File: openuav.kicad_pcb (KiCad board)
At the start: 4 copper layers, 36 x 36 mm, 75 parts, among them J1 Conn_01x01, J10 Conn_01x01, J11 Conn_01x01, J12 Conn_01x01, J13 Conn_01x01, J14 Conn_01x01, J15 Conn_01x01, J16 Conn_01x01, J17 Conn_01x01, J18 Conn_01x01, J19 Conn_01x01, J2 Conn_01x01, J20 Conn_01x01, J21 Conn_01x01, J22 Conn_01x01, J23 Conn_01x01, J24 Conn_01x01, J25 Conn_01x01, J26 Conn_01x01, J27 Conn_01x01, J28 Conn_01x01, J3 Conn_01x01, J30 Conn_01x01, J31 Conn_01x01, J4 Conn_01x01, J5 Conn_01x01, J6 Conn_01x01, J7 Conn_01x01, J8 Conn_01x01, J9 Conn_01x01, J99 USB_C_Receptacle_USB2.0, SW1 SW_Push, SW2 SW_Push, U1 STM32G431CBUx, U2 LPS22HH, U3 LSM6DSR, U4 TPS54302, U6 W25N01GVZEIG, U7 TLV75733PDBV

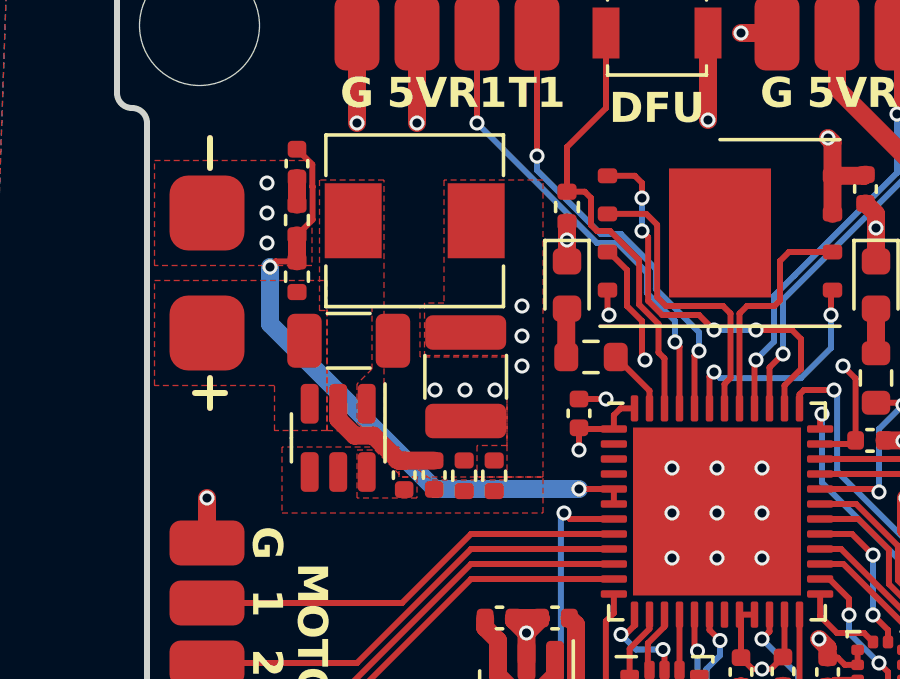
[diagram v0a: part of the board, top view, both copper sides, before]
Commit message: Fix layout for SMPS feedback capacitor
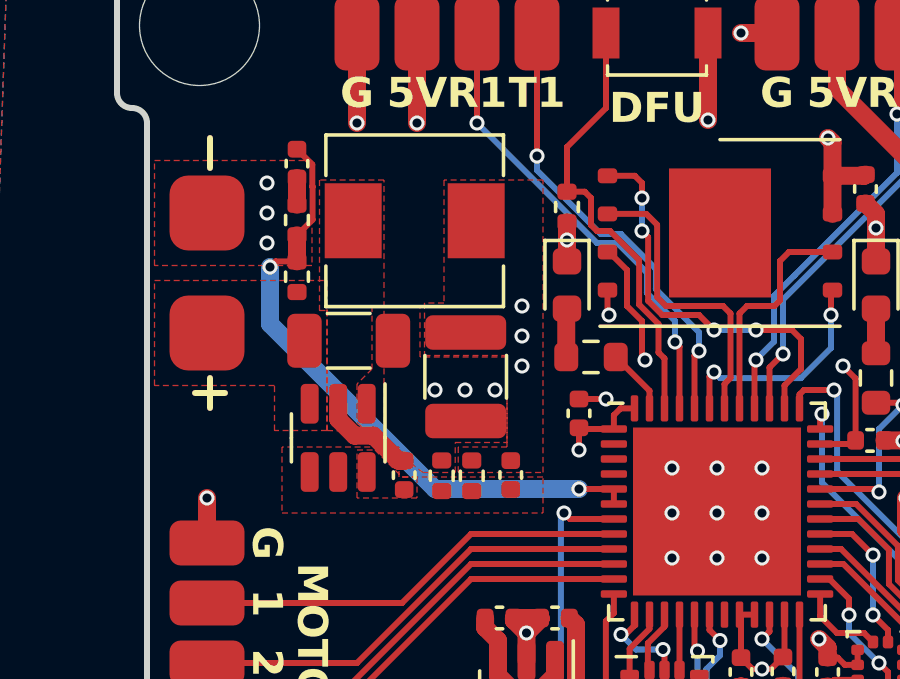
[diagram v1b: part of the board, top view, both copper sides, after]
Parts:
- moved C10 2.55 mm to (143.1, 67.7)
- moved R3 0.75 mm to (141.8, 67.8)
- moved R4 0.75 mm to (140.8, 67.8)
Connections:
- C10 pad 2: Net-(U4-SW) -> +5V
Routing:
- net Net-(U4-SW): track 4.29 -> 3.30 mm
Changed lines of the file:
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@@
   )
   (footprint "Resistor_SMD:R_0402_1005Metric" (layer "F.Cu")
-    (at 141.573 67.758789 90)
+    (at 140.825 67.758789 90)
     (descr "Resistor SMD 0402 (1005 Metric), square (rectangular) end terminal, IPC_7351 nominal, (Body size source: IPC-SM-782 page 72, https://www.pcb-3d.com/wordpress/wp-content/uploads/ipc-sm-782a_amendment_1_and_2.pdf), generated with kicad-footprint-generator")
     (tags "resistor")
@@
   )
   (footprint "Resistor_SMD:R_0402_1005Metric" (layer "F.Cu")
-    (at 142.573 67.758789 -90)
+    (at 141.825 67.758789 -90)
     (descr "Resistor SMD 0402 (1005 Metric), square (rectangular) end terminal, IPC_7351 nominal, (Body size source: IPC-SM-782 page 72, https://www.pcb-3d.com/wordpress/wp-content/uploads/ipc-sm-782a_amendment_1_and_2.pdf), generated with kicad-footprint-generator")
     (tags "resistor")
@@
   )
   (footprint "Capacitor_SMD:C_0402_1005Metric" (layer "F.Cu")
-    (at 140.573 67.733789 90)
+    (at 143.125 67.733789 90)
     (descr "Capacitor SMD 0402 (1005 Metric), square (rectangular) end terminal, IPC_7351 nominal, (Body size source: IPC-SM-782 page 76, https://www.pcb-3d.com/wordpress/wp-content/uploads/ipc-sm-782a_amendment_1_and_2.pdf), generated with kicad-footprint-generator")
     (tags "capacitor")
@@
       (net 7 "Net-(U4-FB)") (pintype "passive"))
     (pad "2" smd roundrect (at 0.48 0 90) (size 0.56 0.62) (layers "F.Cu" "F.Paste" "F.Mask") (roundrect_rratio 0.25)
-      (net 6 "Net-(U4-SW)") (pintype "passive"))
+      (net 9 "+5V") (pintype "passive"))
     (model "${KICAD6_3DMODEL_DIR}/Capacitor_SMD.3dshapes/C_0402_1005Metric.wrl"
       (offset (xyz 0 0 0))
@@
   (segment (start 139.388317 67.258789) (end 138.550817 66.421289) (width 0.6) (layer "F.Cu") (net 6))
   (segment (start 139.578 67.253789) (end 139.573 67.258789) (width 0.6) (layer "F.Cu") (net 6))
-  (segment (start 140.573 67.253789) (end 139.578 67.253789) (width 0.6) (layer "F.Cu") (net 6))
   (segment (start 137.921289 66.421289) (end 137.373 65.873) (width 0.6) (layer "F.Cu") (net 6))
   (segment (start 136 60.613789) (end 135.286211 60.613789) (width 0.2) (layer "F.Cu") (net 8))
@@
         (xy 140.25 63.75)
         (xy 143 63.75)
-        (xy 143 66.75)
-        (xy 142 66.75)
-        (xy 142 67.8)
-        (xy 144.2 67.8)
+        (xy 143 66.8)
+        (xy 141.375 66.8)
+        (xy 141.375 67.65)
+        (xy 144.2 67.65)
       )
     )
@@
         (xy 138 64.7)
         (xy 138 66)
-        (xy 140.5 67.9)
-        (xy 143 67.9)
+        (xy 140.2 67.65)
+        (xy 141.275 67.65)
+        (xy 141.275 66.65)
+        (xy 143 66.65)
         (xy 143 63.8)
         (xy 140.1 63.8)

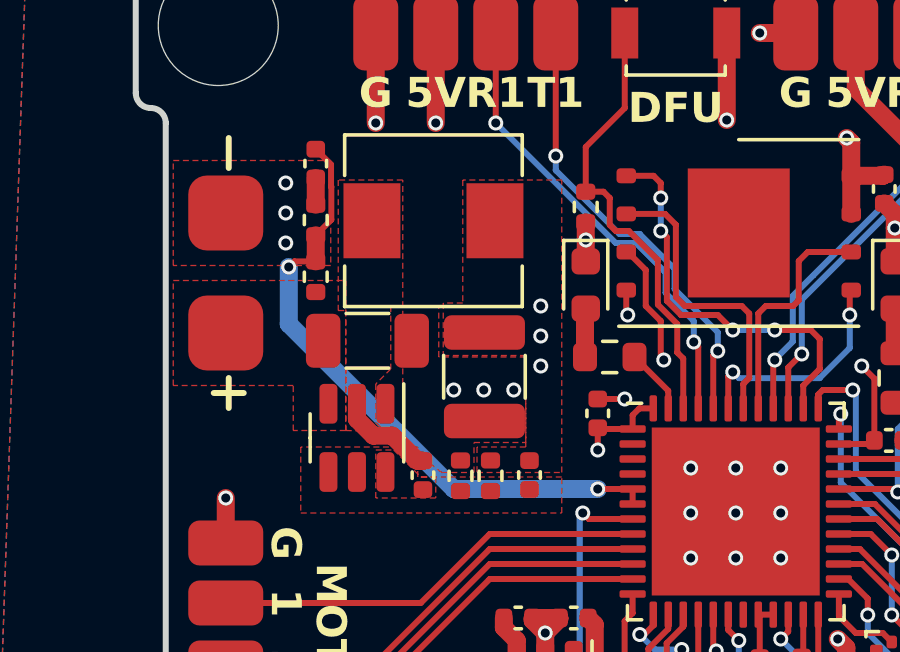
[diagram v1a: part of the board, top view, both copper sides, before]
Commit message: remove copper under inductor
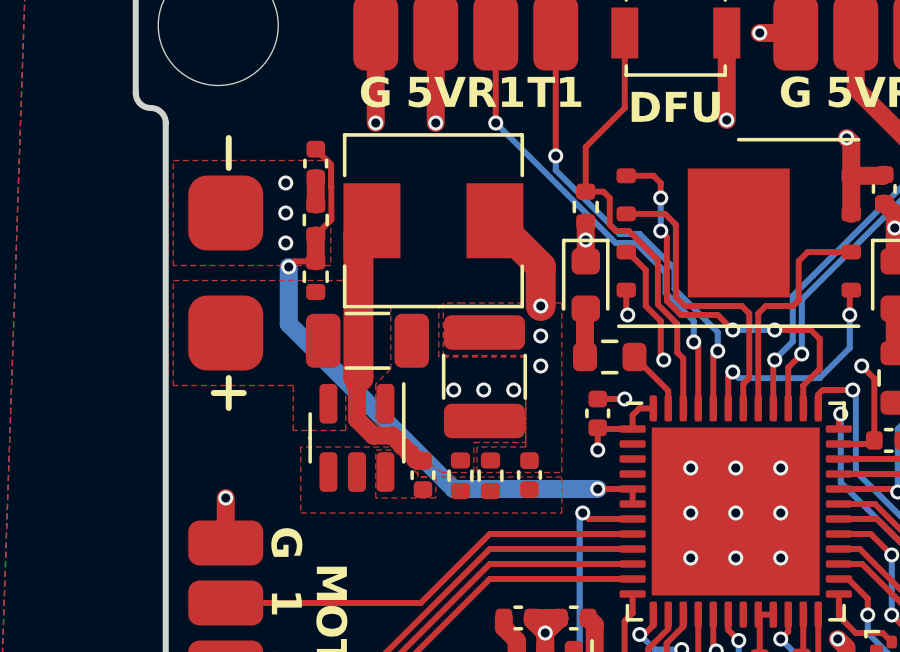
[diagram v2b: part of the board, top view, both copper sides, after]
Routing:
- net Net-(U4-SW): track 3.30 -> 8.70 mm
- net +5V: track 19.5 -> 23.0 mm
- removed copper zone on F.Cu, net Net-(U4-SW)
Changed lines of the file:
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@@
   (segment (start 138.550817 66.421289) (end 137.921289 66.421289) (width 0.6) (layer "F.Cu") (net 6))
   (segment (start 137.373 65.873) (end 137.373 65.358789) (width 0.6) (layer "F.Cu") (net 6))
+  (segment (start 137.423 64.473) (end 137.425 64.475) (width 1) (layer "F.Cu") (net 6))
+  (segment (start 137.873 59.258789) (end 137.423 59.708789) (width 1) (layer "F.Cu") (net 6))
   (segment (start 139.388317 67.258789) (end 138.550817 66.421289) (width 0.6) (layer "F.Cu") (net 6))
   (segment (start 139.578 67.253789) (end 139.573 67.258789) (width 0.6) (layer "F.Cu") (net 6))
+  (segment (start 137.423 59.708789) (end 137.423 64.473) (width 1) (layer "F.Cu") (net 6))
   (segment (start 137.921289 66.421289) (end 137.373 65.873) (width 0.6) (layer "F.Cu") (net 6))
   (segment (start 136 60.613789) (end 135.286211 60.613789) (width 0.2) (layer "F.Cu") (net 8))
@@
   (segment (start 145.4 68.2) (end 140.6 68.2) (width 0.6) (layer "B.Cu") (net 8))
   (segment (start 142.7 73.925) (end 142.7 74.415317) (width 0.6) (layer "F.Cu") (net 9))
+  (segment (start 143.5 60.785789) (end 141.973 59.258789) (width 1) (layer "F.Cu") (net 9))
   (segment (start 144.6 74.415317) (end 144.6 73.925) (width 0.6) (layer "F.Cu") (net 9))
   (segment (start 142.7 73.25) (end 142.7 73.925) (width 0.6) (layer "F.Cu") (net 9))
@@
   (segment (start 140 53) (end 140 56) (width 0.6) (layer "F.Cu") (net 9))
   (segment (start 154 54.85) (end 157.25 58.1) (width 0.6) (layer "F.Cu") (net 9))
+  (segment (start 143.5 62.1) (end 143.5 60.785789) (width 1) (layer "F.Cu") (net 9))
   (segment (start 150 83) (end 150 80.7) (width 0.6) (layer "F.Cu") (net 9))
   (segment (start 144.027817 74.9875) (end 144.6 74.415317) (width 0.6) (layer "F.Cu") (net 9))
@@
     )
   )
-  (zone (net 6) (net_name "Net-(U4-SW)") (layer "F.Cu") (hatch edge 0.5)
-    (priority 2)
-    (connect_pads yes (clearance 0.2))
-    (min_thickness 0.25) (filled_areas_thickness no)
-    (fill yes (thermal_gap 0.5) (thermal_bridge_width 0.5) (smoothing fillet) (radius 0.5))
-    (polygon
-      (pts
-        (xy 138.9 57.9)
-        (xy 136.75 57.9)
-        (xy 136.75 62.25)
-        (xy 137 62.25)
-        (xy 137 66.25)
-        (xy 138.9 66.3)
-      )
-    )
-  )
   (zone (net 3) (net_name "+BATT") (layer "F.Cu") (hatch edge 0.5)
     (priority 1)
@@
     (polygon
       (pts
-        (xy 144.2 57.9)
-        (xy 140.9 57.9)
+        (xy 144.2 62)
         (xy 140.9 62)
         (xy 140.25 62)
@@
       )
     )
+  )
+  (zone (net 0) (net_name "") (layers "F.Cu" "In1.Cu" "In2.Cu" "B.Cu") (hatch edge 0.5)
+    (connect_pads (clearance 0))
+    (min_thickness 0.25) (filled_areas_thickness no)
+    (keepout (tracks allowed) (vias allowed) (pads allowed) (copperpour not_allowed) (footprints allowed))
+    (fill (thermal_gap 0.5) (thermal_bridge_width 0.5))
+    (polygon
+      (pts
+        (xy 136.975 56.425)
+        (xy 136.975 62.1)
+        (xy 142.875 62.1)
+        (xy 142.875 56.425)
+      )
+    )

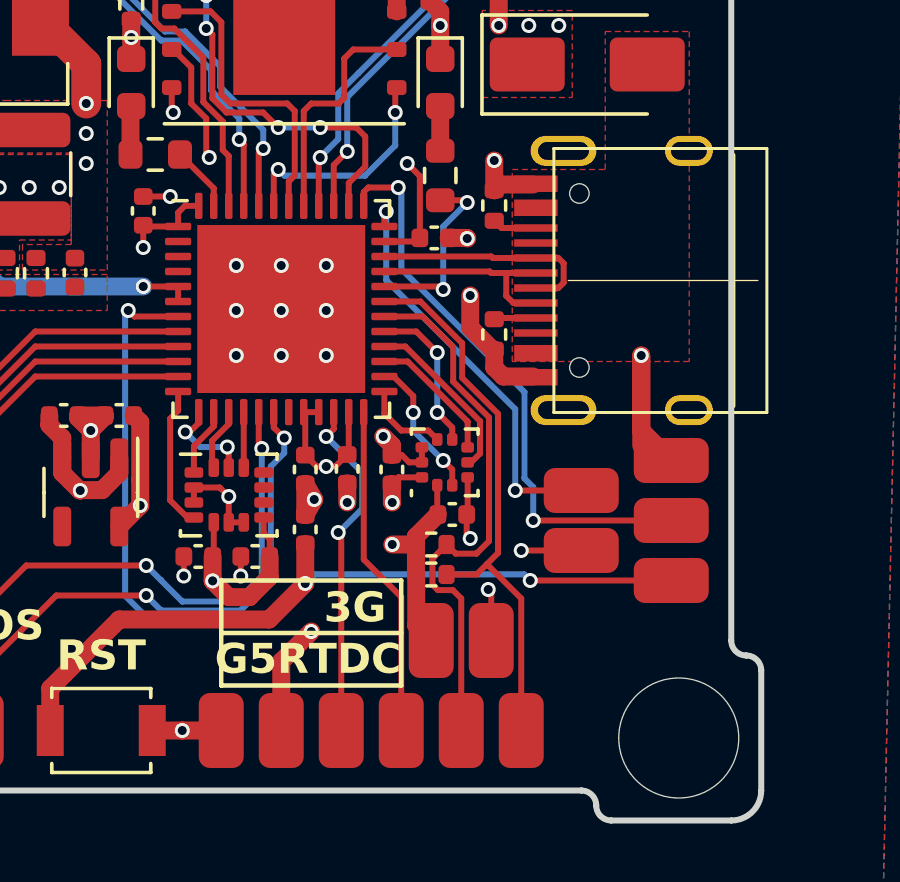
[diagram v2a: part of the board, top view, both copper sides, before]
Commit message: Remove debug port
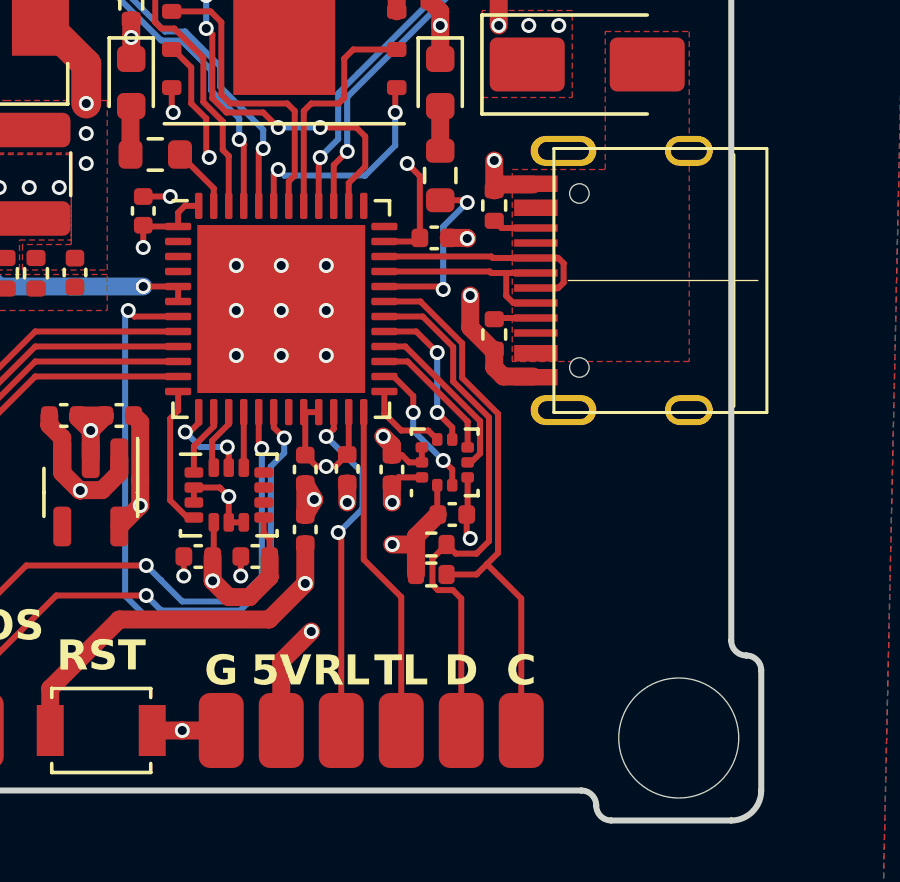
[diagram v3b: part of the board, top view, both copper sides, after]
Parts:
- removed J15, J16, J17, J18, J26, J27, J28: Conn_01x01, footprints:smallpad
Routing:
- net SWCLK: track 19.2 -> 0.00 mm, vias 2 -> 0
- net SWDIO: track 13.8 -> 0.00 mm, vias 2 -> 0
- net NRST: track 43.2 -> 30.8 mm, vias 3 -> 2
- net GND: track 45.1 -> 36.4 mm, vias 36 -> 34
- net +3V3: track 44.4 -> 39.2 mm, vias 11 -> 10
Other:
- board text added: "C"
- board text added: "D"
- board text added: "RL"
- board text added: "TL"
- board text removed: "3G"
- board text removed: "G5RTDC"
